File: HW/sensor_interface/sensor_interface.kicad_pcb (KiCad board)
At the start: 2 copper layers, 22 x 40 mm, 35 parts, among them J1 Berg, J2 Screw_Terminal_01x04, J4 Screw_Terminal, U1 74LVC1G14, U2 MAX31856

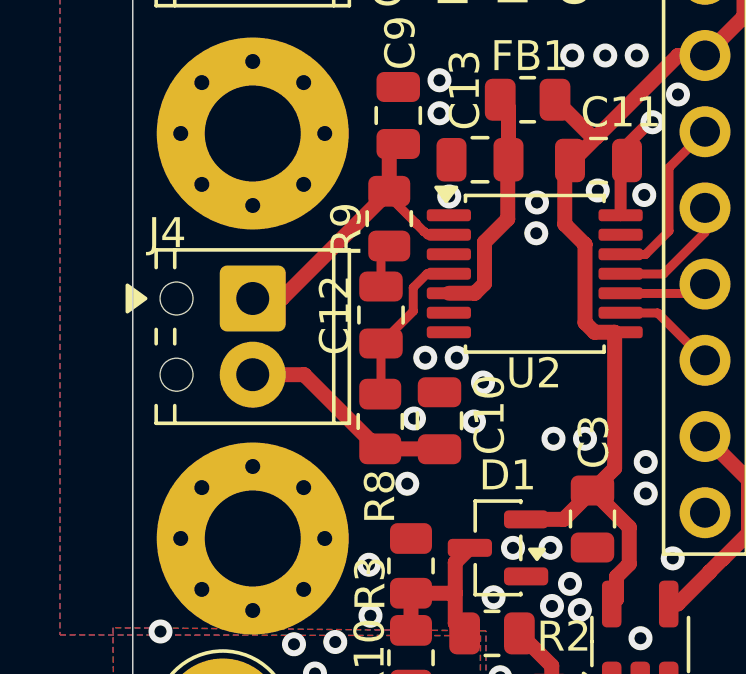
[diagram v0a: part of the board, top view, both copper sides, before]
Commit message: Update sensor_interface.kicad_pcb
Fixed a missing trace/connection to U2 pin 3.
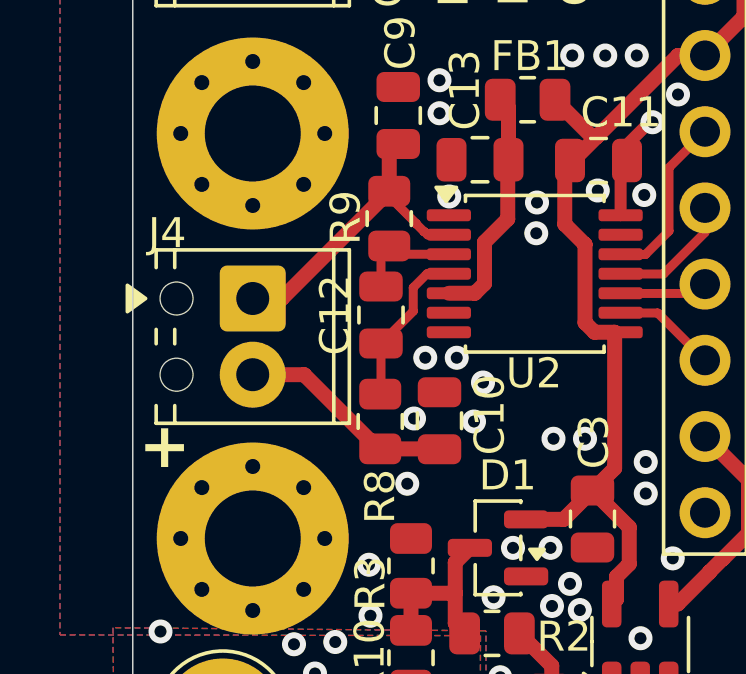
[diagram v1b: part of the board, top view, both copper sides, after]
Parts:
- C12: value 10u -> 100n
- C6: value 2.2n -> 10n
- R4, R6: value 1k -> 10k
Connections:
- net /SPI_TC_CS renamed /~{SPI_TC_CS}
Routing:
- net Net-(U2-T-): track 1.40 -> 3.50 mm
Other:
- board text added: "+"
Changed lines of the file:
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@@
 			)
 		)
-		(property "Description" "Generic connector, single row, 01x09, script generated"
+		(property "Description" "Generic connector, single row, 01x09"
 			(at 0 0 0)
 			(layer "F.Fab")
@@
 			(layers "*.Cu" "*.Mask")
 			(remove_unused_layers no)
-			(net "/SPI_TC_CS")
+			(net "/~{SPI_TC_CS}")
 			(pinfunction "Pin_7_7")
 			(pintype "passive")
@@
 			)
 		)
-		(property "Description" "Unpolarized capacitor"
+		(property "Description" "Generic unpolarized capacitor"
 			(at 0 0 90)
 			(layer "F.Fab")
@@
 			)
 		)
+		(property "Manufacturer" "Kemet"
+			(at 0 0 90)
+			(unlocked yes)
+			(layer "F.Fab")
+			(hide yes)
+			(effects
+				(font
+					(size 1 1)
+					(thickness 0.15)
+				)
+			)
+		)
+		(property "MPN" "C0805C222KAGECAUTO"
+			(at 0 0 90)
+			(unlocked yes)
+			(layer "F.Fab")
+			(hide yes)
+			(effects
+				(font
+					(size 1 1)
+					(thickness 0.15)
+				)
+			)
+		)
 		(property ki_fp_filters "C_*")
 		(sheetname "/")
@@
 			)
 		)
+		(property "Manufacturer" ""
+			(at 0 0 90)
+			(unlocked yes)
+			(layer "F.Fab")
+			(hide yes)
+			(effects
+				(font
+					(size 1 1)
+					(thickness 0.15)
+				)
+			)
+		)
+		(property "MPN" ""
+			(at 0 0 90)
+			(unlocked yes)
+			(layer "F.Fab")
+			(hide yes)
+			(effects
+				(font
+					(size 1 1)
+					(thickness 0.15)
+				)
+			)
+		)
 		(property ki_fp_filters "SOT?23* SOT?553*")
 		(sheetname "/")
@@
 			)
 		)
-		(property "Value" "1k"
+		(property "Value" "10k"
 			(at -2.561116 0 90)
 			(layer "F.Fab")
@@
 			)
 		)
-		(property "Description" "Resistor"
+		(property "Description" "Generic resistor, <= 1%, <= 100 ppm/K"
 			(at 0 0 90)
 			(layer "F.Fab")
@@
 			)
 		)
-		(property "Value" "10u"
+		(property "Value" "100n"
 			(at -0.15 -1.525 90)
 			(layer "F.Fab")
@@
 			)
 		)
-		(property "Value" "2.2n"
+		(property "Value" "10n"
 			(at -2.936116 0.05 90)
 			(layer "F.Fab")
@@
 			)
 		)
-		(property "Description" "Resistor"
+		(property "Description" "Generic Resistor, >= 200 V"
 			(at 0 0 45)
 			(layer "F.Fab")
@@
 			)
 		)
+		(property "Manufacturer" "Vishay"
+			(at 0 0 45)
+			(unlocked yes)
+			(layer "F.Fab")
+			(hide yes)
+			(effects
+				(font
+					(size 1 1)
+					(thickness 0.15)
+				)
+			)
+		)
+		(property "MPN" "CRCW08051M00FKEA"
+			(at 0 0 45)
+			(unlocked yes)
+			(layer "F.Fab")
+			(hide yes)
+			(effects
+				(font
+					(size 1 1)
+					(thickness 0.15)
+				)
+			)
+		)
 		(property ki_fp_filters "R_*")
 		(sheetname "/")
@@
 			)
 		)
+		(property "Manufacturer" "EVVO"
+			(at 0 0 180)
+			(unlocked yes)
+			(layer "F.Fab")
+			(hide yes)
+			(effects
+				(font
+					(size 1 1)
+					(thickness 0.15)
+				)
+			)
+		)
+		(property "MPN" "BAT54S"
+			(at 0 0 180)
+			(unlocked yes)
+			(layer "F.Fab")
+			(hide yes)
+			(effects
+				(font
+					(size 1 1)
+					(thickness 0.15)
+				)
+			)
+		)
 		(property ki_fp_filters "SOT?23*")
 		(sheetname "/")
@@
 			)
 		)
-		(property "Value" "1k"
+		(property "Value" "10k"
 			(at -2.238884 -0.025 90)
 			(layer "F.Fab")
@@
 			)
 		)
+		(property "Manufacturer" "Analog Devices"
+			(at 0 0 0)
+			(unlocked yes)
+			(layer "F.Fab")
+			(hide yes)
+			(effects
+				(font
+					(size 1 1)
+					(thickness 0.15)
+				)
+			)
+		)
+		(property "MPN" "MAX31856MUD+T"
+			(at 0 0 0)
+			(unlocked yes)
+			(layer "F.Fab")
+			(hide yes)
+			(effects
+				(font
+					(size 1 1)
+					(thickness 0.15)
+				)
+			)
+		)
 		(property ki_fp_filters "TSSOP*14*4.4x5mm*P0.65mm*")
 		(sheetname "/")
@@
 			(layers "F.Cu" "F.Mask" "F.Paste")
 			(roundrect_rratio 0.25)
-			(net "/SPI_TC_CS")
+			(net "/~{SPI_TC_CS}")
 			(pinfunction "~{CS}_9")
 			(pintype "input")
@@
 			)
 		)
-		(property "Description" "Unpolarized capacitor"
+		(property "Description" "Unpolarized capacitor, C0G/NP0, 0805, preferably 500 V or 1 kV"
 			(at 0 0 0)
 			(layer "F.Fab")
@@
 			)
 		)
+		(property "Manufacturer" "  YAGEO"
+			(at 0 0 0)
+			(unlocked yes)
+			(layer "F.Fab")
+			(hide yes)
+			(effects
+				(font
+					(size 1 1)
+					(thickness 0.15)
+				)
+			)
+		)
+		(property "MPN" "CC0805JRNPOCBN100"
+			(at 0 0 0)
+			(unlocked yes)
+			(layer "F.Fab")
+			(hide yes)
+			(effects
+				(font
+					(size 1 1)
+					(thickness 0.15)
+				)
+			)
+		)
 		(property ki_fp_filters "C_*")
 		(sheetname "/")
@@
 		(tags "resistor")
 		(property "Reference" "R9"
-			(at 0.3625 1.425 90)
+			(at -0.0375 1.45 90)
 			(layer "F.SilkS")
 			(effects
@@
 		)
 	)
+	(gr_text "+"
+		(at 92.2 92.8 0)
+		(layer "F.SilkS")
+		(effects
+			(font
+				(size 1.5 1.5)
+				(thickness 0.2)
+				(bold yes)
+			)
+			(justify left bottom)
+		)
+	)
 	(gr_text "GND"
 		(at 92.575 93.2 270)
@@
 	)
 	(segment
-		(start 109.4975 87.4825)
-		(end 111.075 89.06)
-		(width 0.3)
-		(layer "F.Cu")
-		(net "/SPI_TC_CS")
-	)
-	(segment
-		(start 108.1875 87.4825)
-		(end 109.4975 87.4825)
-		(width 0.3)
-		(layer "F.Cu")
-		(net "/SPI_TC_CS")
-	)
-	(segment
 		(start 112.525 93.05)
 		(end 111.075 91.6)
@@
 	)
 	(segment
+		(start 100.825 85.525)
+		(end 100.55 85.25)
+		(width 0.3)
+		(layer "F.Cu")
+		(net "Net-(U2-T-)")
+	)
+	(segment
+		(start 102.5375 85.525)
+		(end 100.825 85.525)
+		(width 0.3)
+		(layer "F.Cu")
+		(net "Net-(U2-T-)")
+	)
+	(segment
 		(start 100.275 86.6)
 		(end 100.275 85.2)
@@
 		(net "Net-(U2-AVDD)")
 	)
+	(segment
+		(start 109.4975 87.4825)
+		(end 111.075 89.06)
+		(width 0.3)
+		(layer "F.Cu")
+		(net "/~{SPI_TC_CS}")
+	)
+	(segment
+		(start 108.1875 87.4825)
+		(end 109.4975 87.4825)
+		(width 0.3)
+		(layer "F.Cu")
+		(net "/~{SPI_TC_CS}")
+	)
 	(zone
